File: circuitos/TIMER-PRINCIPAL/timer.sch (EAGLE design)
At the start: 19 parts, among them IC1 MEGA8-P, IC2 7805TV, J1 PWR, K1 JJM1-12V, Q1 16Mhz, T1 BC337, X1 IN, X2 OUT, X3 BOTOEIRA

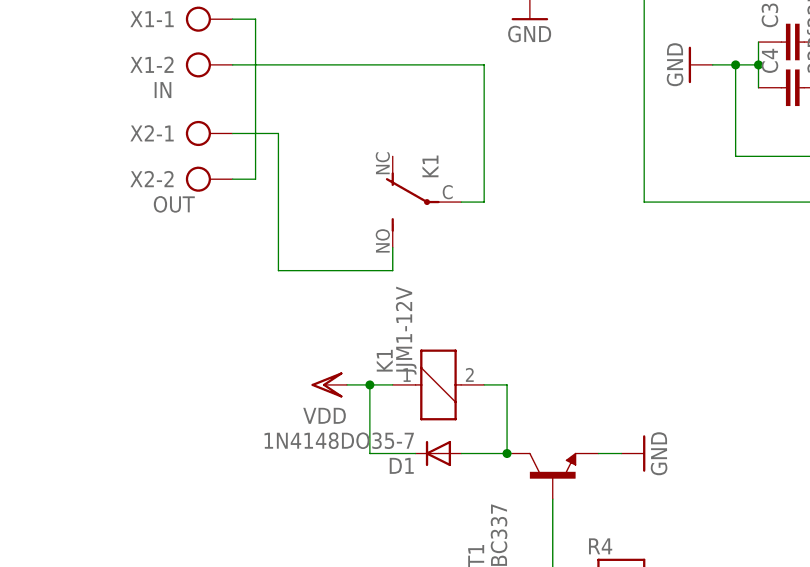
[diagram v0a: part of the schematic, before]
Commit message: Trocado o componente do relé
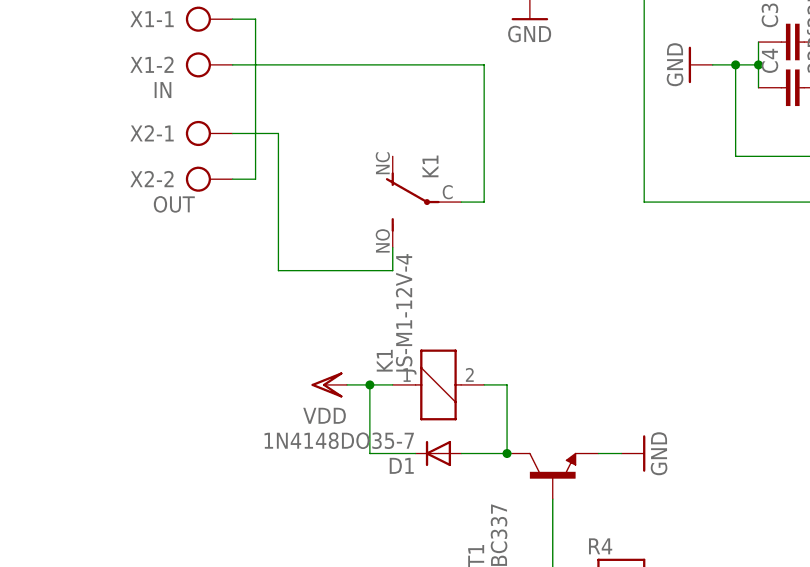
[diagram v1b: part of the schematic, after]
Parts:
- K1: value JJM1-12V -> JS-M1-12V-4; device relay:JJM1-12V -> relay:JS-M1-12V-4
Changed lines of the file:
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@@
 <part name="GND3" library="supply1" deviceset="GND" device=""/>
 <part name="R1" library="rcl" deviceset="R-EU_" device="0204/7" value="10k"/>
-<part name="K1" library="relay" deviceset="JJM1-12V" device=""/>
+<part name="K1" library="relay" deviceset="JS-M1*" device="" technology="-12V-4" value="JS-M1-12V-4"/>
 <part name="T1" library="transistor" deviceset="BC337" device=""/>
 <part name="GND6" library="supply1" deviceset="GND" device=""/>
